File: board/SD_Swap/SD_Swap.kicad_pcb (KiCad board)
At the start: 4 copper layers, 32 x 27 mm, 44 parts, among them J1 USB_C, Q1 Q_Dual_PNP_PNP_E1B1C2E2B2C1, U1 74LVC2G14, U2 RTS5306E, U3 PCB_SD, U4 93AAxxAT, U5 TS3A27518ERTW, U6 SD_SOCKET, U7 AZ1117-3.3, Y1 12MHz

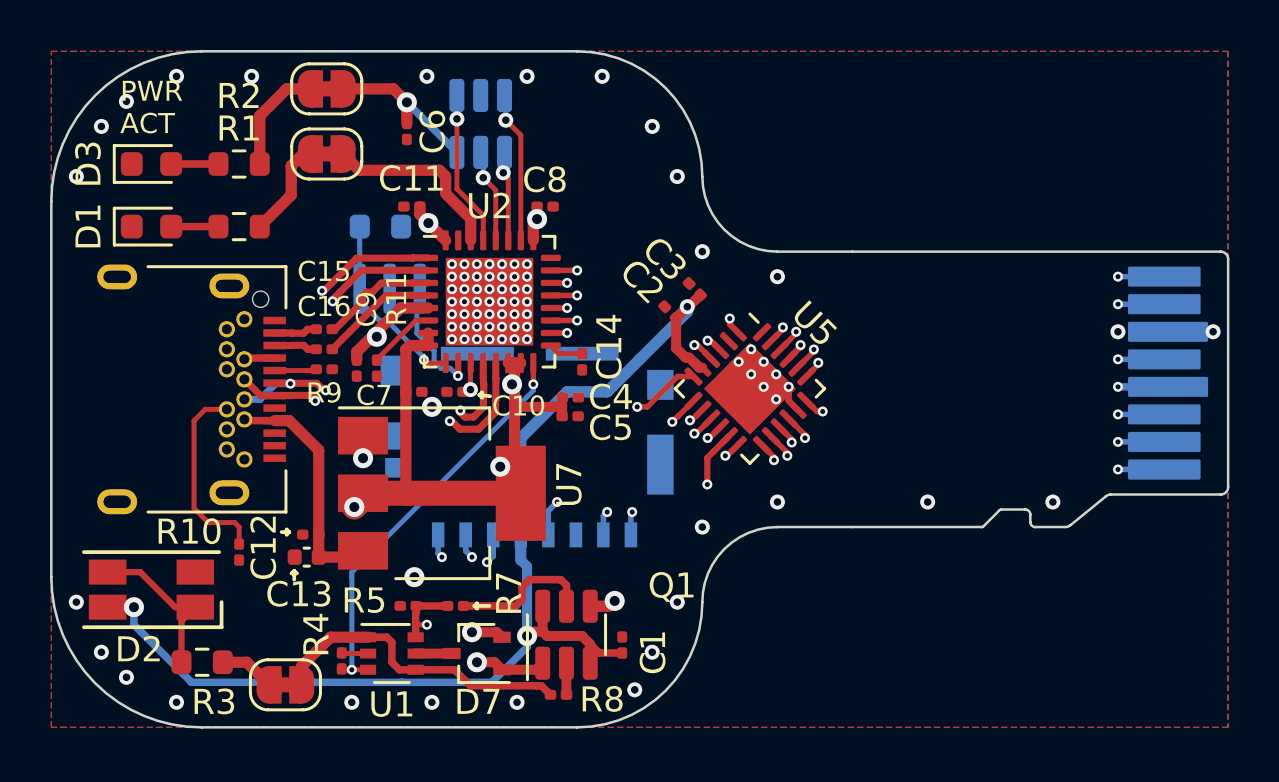
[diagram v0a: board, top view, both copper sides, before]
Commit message: Update silkscreen to include logo and revision number
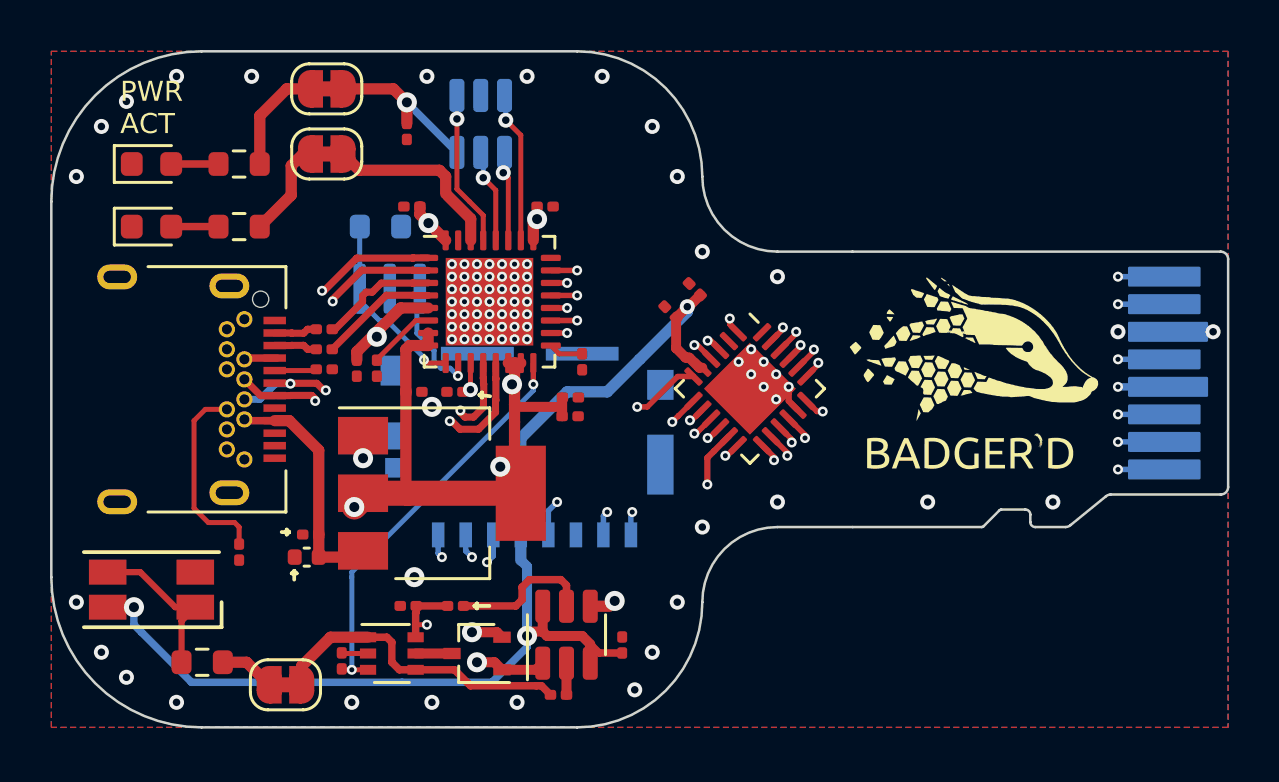
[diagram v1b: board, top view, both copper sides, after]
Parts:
- added G***: LOGO, LOGO, F.Cu at (127.9, 80.9)
- added G***: LOGO, LOGO, B.Cu at (127.4, 81.2)
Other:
- board text added: "SDWire3 Rev 1.0"
